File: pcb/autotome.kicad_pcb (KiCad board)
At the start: 2 copper layers, 137 x 112.3 mm, 65 parts, among them SW1 SW_PUSH, SW10 SW_PUSH, SW11 SW_PUSH, SW12 SW_PUSH, SW13 SW_PUSH, SW14 SW_PUSH, SW15 SW_PUSH, SW16 SW_PUSH, SW17 SW_PUSH, SW18 SW_PUSH, SW19 SW_PUSH, SW2 SW_PUSH, SW20 SW_PUSH, SW21 SW_PUSH, SW22 SW_PUSH, SW23 SW_PUSH, SW24 SW_PUSH, SW25 RotaryEncoder_Switch, SW27 SW_PUSH, SW28 SW_PUSH, SW29 SW_PUSH, SW3 SW_PUSH, SW30 SW_PUSH, SW31 SW_SPDT, SW4 SW_PUSH, SW5 SW_PUSH, SW6 SW_PUSH, SW7 SW_PUSH, SW8 SW_PUSH, SW9 SW_PUSH, U1 ProMicro

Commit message: add mousebites
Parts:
- added REF**: MouseBite-Slot_2.0x2.0mm_inset_D0.5mm_P0.85mm_4h_Trace, Panelization:MouseBite-Slot_2.0x2.0mm_inset_D0.5mm_P0.85mm_4h_Trace, F.Cu at (20.8, 56.6)
- added REF**: MouseBite-Slot_2.0x2.0mm_inset_D0.5mm_P0.85mm_4h_Trace, Panelization:MouseBite-Slot_2.0x2.0mm_inset_D0.5mm_P0.85mm_4h_Trace, F.Cu at (94.8, 56.6)
- added REF**: MouseBite-Slot_2.0x2.0mm_inset_D0.5mm_P0.85mm_4h_Trace, Panelization:MouseBite-Slot_2.0x2.0mm_inset_D0.5mm_P0.85mm_4h_Trace, F.Cu at (56.9, 56.6)
- added REF**: MouseBite-Slot_2.0x2.0mm_inset_D0.5mm_P0.85mm_4h_Trace, Panelization:MouseBite-Slot_2.0x2.0mm_inset_D0.5mm_P0.85mm_4h_Trace, F.Cu at (130.9, 56.6)
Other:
- outline, holes or cut-outs redrawn

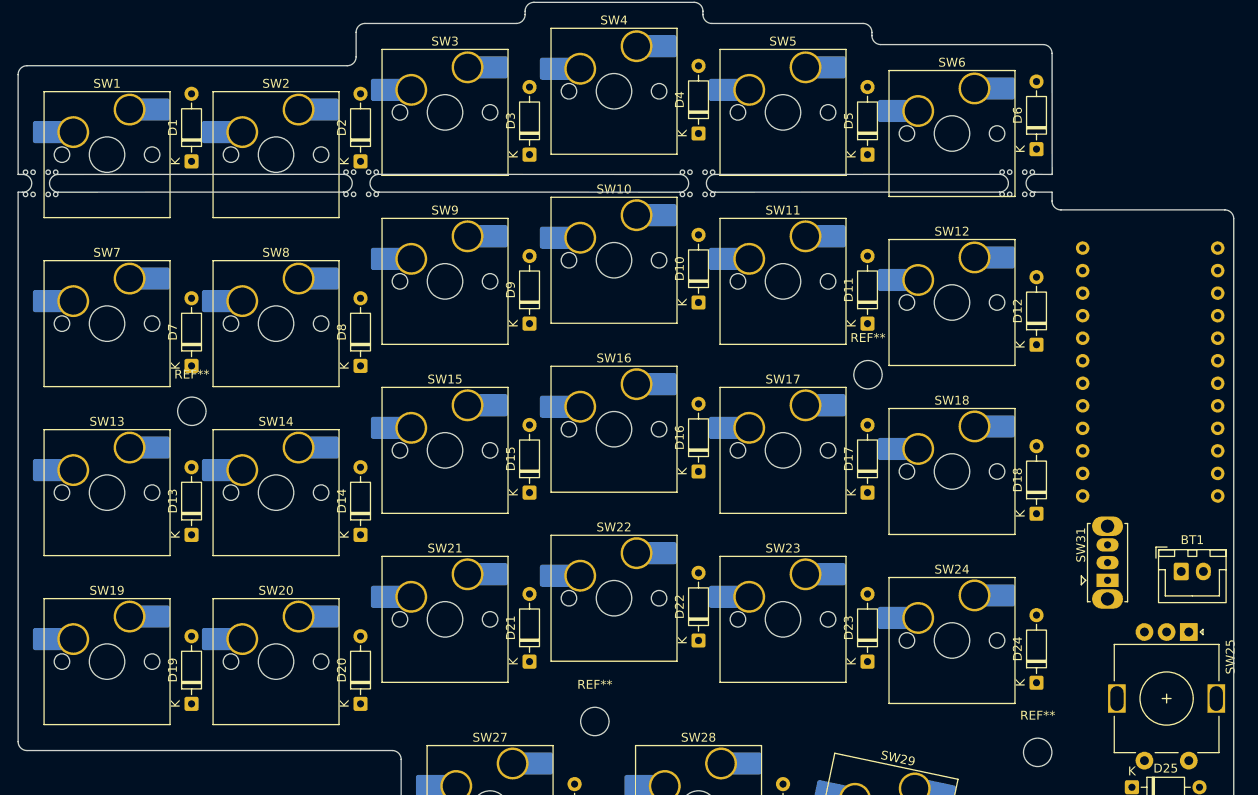
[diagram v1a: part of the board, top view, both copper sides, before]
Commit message: improve cutout shape and move mousebites as needed
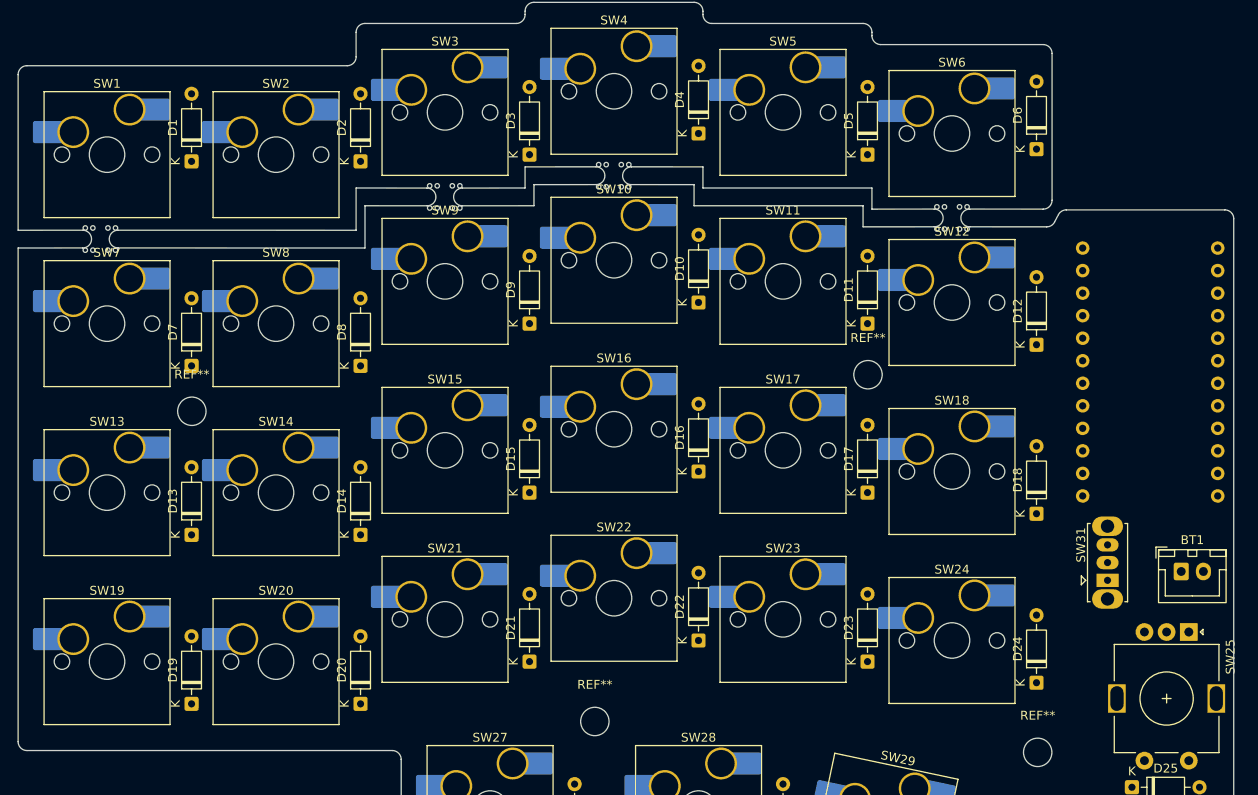
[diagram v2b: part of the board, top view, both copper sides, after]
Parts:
- removed the REF** at (20.8, 56.6)
- removed the REF** at (94.8, 56.6)
- removed the REF** at (56.9, 56.6)
- removed the REF** at (130.9, 56.6)
- added REF**: MouseBite-Slot_2.0x2.0mm_inset_D0.5mm_P0.85mm_4h_Trace, Panelization:MouseBite-Slot_2.0x2.0mm_inset_D0.5mm_P0.85mm_4h_Trace, F.Cu at (123.5, 60.5)
- added REF**: MouseBite-Slot_2.0x2.0mm_inset_D0.5mm_P0.85mm_4h_Trace, Panelization:MouseBite-Slot_2.0x2.0mm_inset_D0.5mm_P0.85mm_4h_Trace, F.Cu at (85.4, 55.8)
- added REF**: MouseBite-Slot_2.0x2.0mm_inset_D0.5mm_P0.85mm_4h_Trace, Panelization:MouseBite-Slot_2.0x2.0mm_inset_D0.5mm_P0.85mm_4h_Trace, F.Cu at (27.5, 62.9)
- added REF**: MouseBite-Slot_2.0x2.0mm_inset_D0.5mm_P0.85mm_4h_Trace, Panelization:MouseBite-Slot_2.0x2.0mm_inset_D0.5mm_P0.85mm_4h_Trace, F.Cu at (66.3, 58.2)
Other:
- outline, holes or cut-outs redrawn

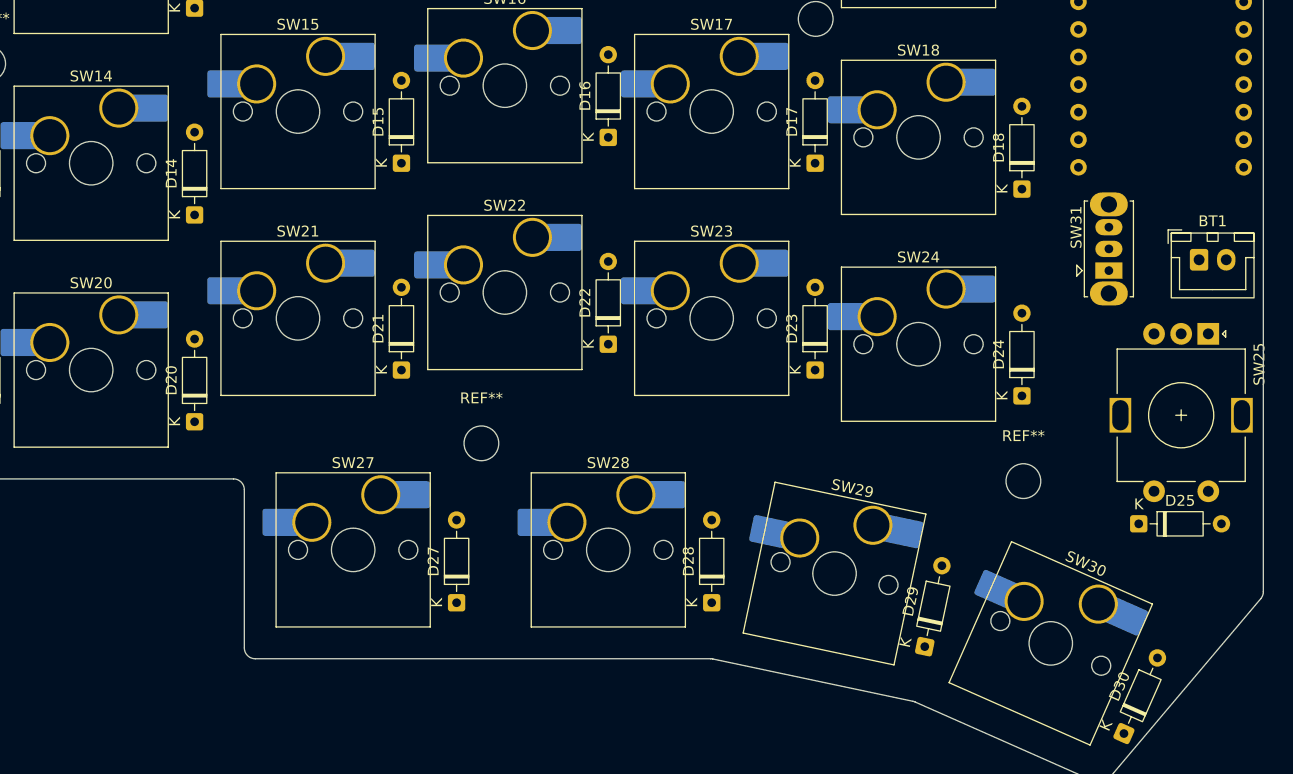
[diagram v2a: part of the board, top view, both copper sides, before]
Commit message: fix button number order in schematic, update pcb
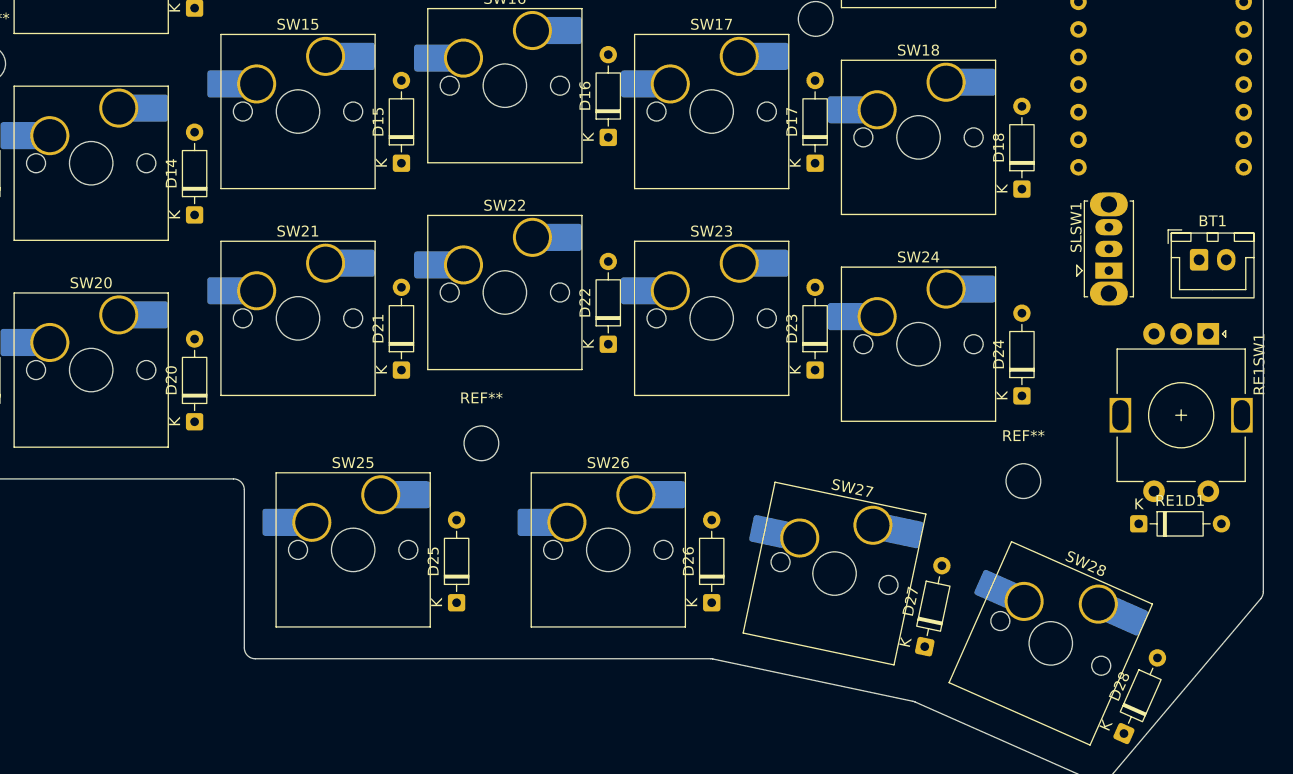
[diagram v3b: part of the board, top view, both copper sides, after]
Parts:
- renumbered D27 to D25, D28 to D26, D29 to D27, D30 to D28, D25 to RE1D1, SW25 to RE1SW1, SW31 to SLSW1, SW27 to SW25, SW28 to SW26, SW29 to SW27, SW30 to SW28
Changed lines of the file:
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@@
 		(descr "Diode, DO-35_SOD27 series, Axial, Horizontal, pin pitch=7.62mm, length*diameter=4*2mm^2, http://www.diodes.com/_files/packages/DO-35.pdf")
 		(tags "Diode DO-35_SOD27 series Axial Horizontal pin pitch 7.62mm  length 4mm diameter 2mm")
-		(property "Reference" "D25"
+		(property "Reference" "RE1D1"
 			(at 3.81 -2.12 0)
 			(layer "F.SilkS")
@@
 			(layers "*.Cu" "*.Mask")
 			(remove_unused_layers no)
-			(net "Net-(D25-A)")
+			(net "Net-(RE1D1-A)")
 			(pinfunction "A_2")
 			(pintype "passive")
@@
 		(descr "Diode, DO-35_SOD27 series, Axial, Horizontal, pin pitch=7.62mm, length*diameter=4*2mm^2, http://www.diodes.com/_files/packages/DO-35.pdf")
 		(tags "Diode DO-35_SOD27 series Axial Horizontal pin pitch 7.62mm  length 4mm diameter 2mm")
-		(property "Reference" "D30"
+		(property "Reference" "D28"
 			(at 3.81 -2.12 66.12)
 			(layer "F.SilkS")
@@
 			(layers "*.Cu" "*.Mask")
 			(remove_unused_layers no)
-			(net "Net-(D30-A)")
+			(net "Net-(D28-A)")
 			(pinfunction "A_2")
 			(pintype "passive")
@@
 		(descr "Alps rotary encoder, EC11E... with switch, vertical shaft, http://www.alps.com/prod/info/E/HTML/Encoder/Incremental/EC11/EC11E15204A3.html")
 		(tags "rotary encoder")
-		(property "Reference" "SW25"
+		(property "Reference" "RE1SW1"
 			(at 2.8 -4.7 270)
 			(layer "F.SilkS")
@@
 			(layers "*.Cu" "*.Mask")
 			(remove_unused_layers no)
-			(net "Net-(D25-A)")
+			(net "Net-(RE1D1-A)")
 			(pinfunction "S2_S2")
 			(pintype "passive")
@@
 		(descr "Kailh keyswitch Hotswap Socket plated holes Keycap 1.00u")
 		(tags "Kailh Keyboard Keyswitch Switch Hotswap Socket Plated Relief Cutout Keycap 1.00u")
-		(property "Reference" "SW30"
+		(property "Reference" "SW28"
 			(at 0 -7.999999 156.12)
 			(layer "F.SilkS")
@@
 			(layers "*.Cu" "*.Mask")
 			(remove_unused_layers no)
-			(net "Net-(D30-A)")
+			(net "Net-(D28-A)")
 			(pinfunction "2_2")
 			(pintype "passive")
@@
 			(layers "B.Cu")
 			(roundrect_rratio 0.1)
-			(net "Net-(D30-A)")
+			(net "Net-(D28-A)")
 			(pinfunction "2_2")
 			(pintype "passive")
@@
 		(descr "Kailh keyswitch Hotswap Socket plated holes Keycap 1.00u")
 		(tags "Kailh Keyboard Keyswitch Switch Hotswap Socket Plated Relief Cutout Keycap 1.00u")
-		(property "Reference" "SW29"
+		(property "Reference" "SW27"
 			(at 0 -8 168.06)
 			(layer "F.SilkS")
@@
 			(layers "*.Cu" "*.Mask")
 			(remove_unused_layers no)
-			(net "Net-(D29-A)")
+			(net "Net-(D27-A)")
 			(pinfunction "2_2")
 			(pintype "passive")
@@
 			(layers "B.Cu")
 			(roundrect_rratio 0.1)
-			(net "Net-(D29-A)")
+			(net "Net-(D27-A)")
 			(pinfunction "2_2")
 			(pintype "passive")
@@
 		(descr "Kailh keyswitch Hotswap Socket plated holes Keycap 1.00u")
 		(tags "Kailh Keyboard Keyswitch Switch Hotswap Socket Plated Relief Cutout Keycap 1.00u")
-		(property "Reference" "SW28"
+		(property "Reference" "SW26"
 			(at 0 -8 0)
 			(layer "F.SilkS")
@@
 			(layers "*.Cu" "*.Mask")
 			(remove_unused_layers no)
-			(net "Net-(D28-A)")
+			(net "Net-(D26-A)")
 			(pinfunction "2_2")
 			(pintype "passive")
@@
 			(layers "B.Cu")
 			(roundrect_rratio 0.1)
-			(net "Net-(D28-A)")
+			(net "Net-(D26-A)")
 			(pinfunction "2_2")
 			(pintype "passive")
@@
 		(descr "Diode, DO-35_SOD27 series, Axial, Horizontal, pin pitch=7.62mm, length*diameter=4*2mm^2, http://www.diodes.com/_files/packages/DO-35.pdf")
 		(tags "Diode DO-35_SOD27 series Axial Horizontal pin pitch 7.62mm  length 4mm diameter 2mm")
-		(property "Reference" "D29"
+		(property "Reference" "D27"
 			(at 3.81 -2.12 78.06)
 			(layer "F.SilkS")
@@
 			(layers "*.Cu" "*.Mask")
 			(remove_unused_layers no)
-			(net "Net-(D29-A)")
+			(net "Net-(D27-A)")
 			(pinfunction "A_2")
 			(pintype "passive")
@@
 		(descr "Diode, DO-35_SOD27 series, Axial, Horizontal, pin pitch=7.62mm, length*diameter=4*2mm^2, http://www.diodes.com/_files/packages/DO-35.pdf")
 		(tags "Diode DO-35_SOD27 series Axial Horizontal pin pitch 7.62mm  length 4mm diameter 2mm")
-		(property "Reference" "D27"
+		(property "Reference" "D25"
 			(at 3.81 -2.12 90)
 			(layer "F.SilkS")
@@
 			(layers "*.Cu" "*.Mask")
 			(remove_unused_layers no)
-			(net "Net-(D27-A)")
+			(net "Net-(D25-A)")
 			(pinfunction "A_2")
 			(pintype "passive")
@@
 		(descr "CuK miniature slide switch, OS series, SPDT, https://www.ckswitches.com/media/1428/os.pdf")
 		(tags "switch SPDT")
-		(property "Reference" "SW31"
+		(property "Reference" "SLSW1"
 			(at 3.99 -2.99 90)
 			(layer "F.SilkS")
@@
 			(layers "*.Cu" "*.Mask")
 			(remove_unused_layers no)
-			(net "unconnected-(SW31-A-Pad1)")
+			(net "unconnected-(SLSW1-A-Pad1)")
 			(pinfunction "A_1")
 			(pintype "passive")
@@
 		(descr "Kailh keyswitch Hotswap Socket plated holes Keycap 1.00u")
 		(tags "Kailh Keyboard Keyswitch Switch Hotswap Socket Plated Relief Cutout Keycap 1.00u")
-		(property "Reference" "SW27"
+		(property "Reference" "SW25"
 			(at 0 -8 0)
 			(layer "F.SilkS")
@@
 			(layers "*.Cu" "*.Mask")
 			(remove_unused_layers no)
-			(net "Net-(D27-A)")
+			(net "Net-(D25-A)")
 			(pinfunction "2_2")
 			(pintype "passive")
@@
 			(layers "B.Cu")
 			(roundrect_rratio 0.1)
-			(net "Net-(D27-A)")
+			(net "Net-(D25-A)")
 			(pinfunction "2_2")
 			(pintype "passive")
@@
 		(descr "Diode, DO-35_SOD27 series, Axial, Horizontal, pin pitch=7.62mm, length*diameter=4*2mm^2, http://www.diodes.com/_files/packages/DO-35.pdf")
 		(tags "Diode DO-35_SOD27 series Axial Horizontal pin pitch 7.62mm  length 4mm diameter 2mm")
-		(property "Reference" "D28"
+		(property "Reference" "D26"
 			(at 3.81 -2.12 90)
 			(layer "F.SilkS")
@@
 			(layers "*.Cu" "*.Mask")
 			(remove_unused_layers no)
-			(net "Net-(D28-A)")
+			(net "Net-(D26-A)")
 			(pinfunction "A_2")
 			(pintype "passive")
@@
 			(at 0 -8 0)
 			(layer "F.SilkS")
+			(hide yes)
 			(effects
 				(font

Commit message: place right half keys on pcb
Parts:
- added BT2: Battery_Cell, Connector_JST:JST_XH_B2B-XH-A_1x02_P2.50mm_Vertical, F.Cu at (396.0, 119.4)
- added D29: 1N4148, Diode_THT:D_DO-35_SOD27_P7.62mm_Horizontal, F.Cu at (209.2, 54.8)
- added D30: 1N4148, Diode_THT:D_DO-35_SOD27_P7.62mm_Horizontal, F.Cu at (228.3, 52.4)
- added D31: 1N4148, Diode_THT:D_DO-35_SOD27_P7.62mm_Horizontal, F.Cu at (247.3, 50.0)
- added D32: 1N4148, Diode_THT:D_DO-35_SOD27_P7.62mm_Horizontal, F.Cu at (266.4, 52.4)
- added D33: 1N4148, Diode_THT:D_DO-35_SOD27_P7.62mm_Horizontal, F.Cu at (285.4, 57.2)
- added D34: 1N4148, Diode_THT:D_DO-35_SOD27_P7.62mm_Horizontal, F.Cu at (304.5, 57.2)
- added D35: 1N4148, Diode_THT:D_DO-35_SOD27_P7.62mm_Horizontal, F.Cu at (209.2, 73.8)
- added D36: 1N4148, Diode_THT:D_DO-35_SOD27_P7.62mm_Horizontal, F.Cu at (228.3, 71.4)
- added D37: 1N4148, Diode_THT:D_DO-35_SOD27_P7.62mm_Horizontal, F.Cu at (247.3, 69.1)
- added D38: 1N4148, Diode_THT:D_DO-35_SOD27_P7.62mm_Horizontal, F.Cu at (266.4, 71.4)
- added D39: 1N4148, Diode_THT:D_DO-35_SOD27_P7.62mm_Horizontal, F.Cu at (285.4, 76.2)
- added D40: 1N4148, Diode_THT:D_DO-35_SOD27_P7.62mm_Horizontal, F.Cu at (304.5, 76.2)
- added D41: 1N4148, Diode_THT:D_DO-35_SOD27_P7.62mm_Horizontal, F.Cu at (209.2, 92.9)
- added D42: 1N4148, Diode_THT:D_DO-35_SOD27_P7.62mm_Horizontal, F.Cu at (228.3, 90.5)
- added D43: 1N4148, Diode_THT:D_DO-35_SOD27_P7.62mm_Horizontal, F.Cu at (247.3, 88.1)
- added D44: 1N4148, Diode_THT:D_DO-35_SOD27_P7.62mm_Horizontal, F.Cu at (266.4, 90.5)
- added D45: 1N4148, Diode_THT:D_DO-35_SOD27_P7.62mm_Horizontal, F.Cu at (285.4, 95.3)
- added D46: 1N4148, Diode_THT:D_DO-35_SOD27_P7.62mm_Horizontal, F.Cu at (304.5, 95.3)
- added D47: 1N4148, Diode_THT:D_DO-35_SOD27_P7.62mm_Horizontal, F.Cu at (209.2, 111.9)
- added D48: 1N4148, Diode_THT:D_DO-35_SOD27_P7.62mm_Horizontal, F.Cu at (228.3, 109.5)
- added D49: 1N4148, Diode_THT:D_DO-35_SOD27_P7.62mm_Horizontal, F.Cu at (247.3, 107.2)
- added D50: 1N4148, Diode_THT:D_DO-35_SOD27_P7.62mm_Horizontal, F.Cu at (266.4, 109.5)
- added D51: 1N4148, Diode_THT:D_DO-35_SOD27_P7.62mm_Horizontal, F.Cu at (285.4, 114.3)
- added D52: 1N4148, Diode_THT:D_DO-35_SOD27_P7.62mm_Horizontal, F.Cu at (304.5, 114.3)
- added D53: 1N4148, Diode_THT:D_DO-35_SOD27_P7.62mm_Horizontal, F.Cu at (198.8, 136.6)
- added D54: 1N4148, Diode_THT:D_DO-35_SOD27_P7.62mm_Horizontal, F.Cu at (218.1, 132.5)
- added D55: 1N4148, Diode_THT:D_DO-35_SOD27_P7.62mm_Horizontal, F.Cu at (237.8, 132.4)
- added D56: 1N4148, Diode_THT:D_DO-35_SOD27_P7.62mm_Horizontal, F.Cu at (261.3, 132.4)
- added RE1D2: 1N4148, Diode_THT:D_DO-35_SOD27_P7.62mm_Horizontal, F.Cu at (409.3, 135.7)
- added RE1SW2: RotaryEncoder_Switch, autotome_library:RotaryEncoder_Alps_EC11E-Switch_Vertical_H20mm, F.Cu at (376.0, 114.7)
- added SLSW2: SW_SPDT, Button_Switch_THT:SW_Slide_SPDT_Straight_CK_OS102011MS2Q, F.Cu at (396.5, 113.1)
- added SW29: SW_PUSH, PCM_Switch_Keyboard_Hotswap_Kailh:SW_Hotswap_Kailh_MX_Plated_1.00u, F.Cu at (199.7, 50.0)
- added SW30: SW_PUSH, PCM_Switch_Keyboard_Hotswap_Kailh:SW_Hotswap_Kailh_MX_Plated_1.00u, F.Cu at (218.8, 47.6)
- added SW31: SW_PUSH, PCM_Switch_Keyboard_Hotswap_Kailh:SW_Hotswap_Kailh_MX_Plated_1.00u, F.Cu at (237.8, 45.2)
- added SW32: SW_PUSH, PCM_Switch_Keyboard_Hotswap_Kailh:SW_Hotswap_Kailh_MX_Plated_1.00u, F.Cu at (256.9, 47.6)
- added SW33: SW_PUSH, PCM_Switch_Keyboard_Hotswap_Kailh:SW_Hotswap_Kailh_MX_Plated_1.00u, F.Cu at (275.9, 52.4)
- added SW34: SW_PUSH, PCM_Switch_Keyboard_Hotswap_Kailh:SW_Hotswap_Kailh_MX_Plated_1.00u, F.Cu at (295.0, 52.4)
- added SW35: SW_PUSH, PCM_Switch_Keyboard_Hotswap_Kailh:SW_Hotswap_Kailh_MX_Plated_1.00u, F.Cu at (199.7, 69.1)
- added SW36: SW_PUSH, PCM_Switch_Keyboard_Hotswap_Kailh:SW_Hotswap_Kailh_MX_Plated_1.00u, F.Cu at (218.8, 66.7)
- added SW37: SW_PUSH, PCM_Switch_Keyboard_Hotswap_Kailh:SW_Hotswap_Kailh_MX_Plated_1.00u, F.Cu at (237.8, 64.3)
- added SW38: SW_PUSH, PCM_Switch_Keyboard_Hotswap_Kailh:SW_Hotswap_Kailh_MX_Plated_1.00u, F.Cu at (256.9, 66.7)
- added SW39: SW_PUSH, PCM_Switch_Keyboard_Hotswap_Kailh:SW_Hotswap_Kailh_MX_Plated_1.00u, F.Cu at (275.9, 71.4)
- added SW40: SW_PUSH, PCM_Switch_Keyboard_Hotswap_Kailh:SW_Hotswap_Kailh_MX_Plated_1.00u, F.Cu at (295.0, 71.4)
- added SW41: SW_PUSH, PCM_Switch_Keyboard_Hotswap_Kailh:SW_Hotswap_Kailh_MX_Plated_1.00u, F.Cu at (199.7, 88.1)
- added SW42: SW_PUSH, PCM_Switch_Keyboard_Hotswap_Kailh:SW_Hotswap_Kailh_MX_Plated_1.00u, F.Cu at (218.8, 85.7)
- added SW43: SW_PUSH, PCM_Switch_Keyboard_Hotswap_Kailh:SW_Hotswap_Kailh_MX_Plated_1.00u, F.Cu at (237.8, 83.3)
- added SW44: SW_PUSH, PCM_Switch_Keyboard_Hotswap_Kailh:SW_Hotswap_Kailh_MX_Plated_1.00u, F.Cu at (256.9, 85.7)
- added SW45: SW_PUSH, PCM_Switch_Keyboard_Hotswap_Kailh:SW_Hotswap_Kailh_MX_Plated_1.00u, F.Cu at (275.9, 90.5)
- added SW46: SW_PUSH, PCM_Switch_Keyboard_Hotswap_Kailh:SW_Hotswap_Kailh_MX_Plated_1.00u, F.Cu at (295.0, 90.5)
- added SW47: SW_PUSH, PCM_Switch_Keyboard_Hotswap_Kailh:SW_Hotswap_Kailh_MX_Plated_1.00u, F.Cu at (199.7, 107.2)
- added SW48: SW_PUSH, PCM_Switch_Keyboard_Hotswap_Kailh:SW_Hotswap_Kailh_MX_Plated_1.00u, F.Cu at (218.8, 104.8)
- added SW49: SW_PUSH, PCM_Switch_Keyboard_Hotswap_Kailh:SW_Hotswap_Kailh_MX_Plated_1.00u, F.Cu at (237.8, 102.4)
- added SW50: SW_PUSH, PCM_Switch_Keyboard_Hotswap_Kailh:SW_Hotswap_Kailh_MX_Plated_1.00u, F.Cu at (256.9, 104.8)
- added SW51: SW_PUSH, PCM_Switch_Keyboard_Hotswap_Kailh:SW_Hotswap_Kailh_MX_Plated_1.00u, F.Cu at (275.9, 109.5)
- added SW52: SW_PUSH, PCM_Switch_Keyboard_Hotswap_Kailh:SW_Hotswap_Kailh_MX_Plated_1.00u, F.Cu at (295.0, 109.5)
- added SW53: SW_PUSH, PCM_Switch_Keyboard_Hotswap_Kailh:SW_Hotswap_Kailh_MX_Plated_1.00u, F.Cu at (187.6, 134.8)
- added SW54: SW_PUSH, PCM_Switch_Keyboard_Hotswap_Kailh:SW_Hotswap_Kailh_MX_Plated_1.00u, F.Cu at (207.5, 128.4)
- added SW55: SW_PUSH, PCM_Switch_Keyboard_Hotswap_Kailh:SW_Hotswap_Kailh_MX_Plated_1.00u, F.Cu at (228.3, 126.2)
- added SW56: SW_PUSH, PCM_Switch_Keyboard_Hotswap_Kailh:SW_Hotswap_Kailh_MX_Plated_1.00u, F.Cu at (251.8, 126.2)
- added U2: ProMicro, autotome_library:NiceNano, F.Cu at (435.0, 58.1)
